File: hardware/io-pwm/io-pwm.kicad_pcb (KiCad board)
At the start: 2 copper layers, 60 x 60 mm, 30 parts, among them J1 IO EXTENSION, J2 PWM_OUT, J5 12V_A, J6 12V_B, U1 LM317T, U2 74LS164, U3 TLC7226A, U4 LM339, U5 LM555

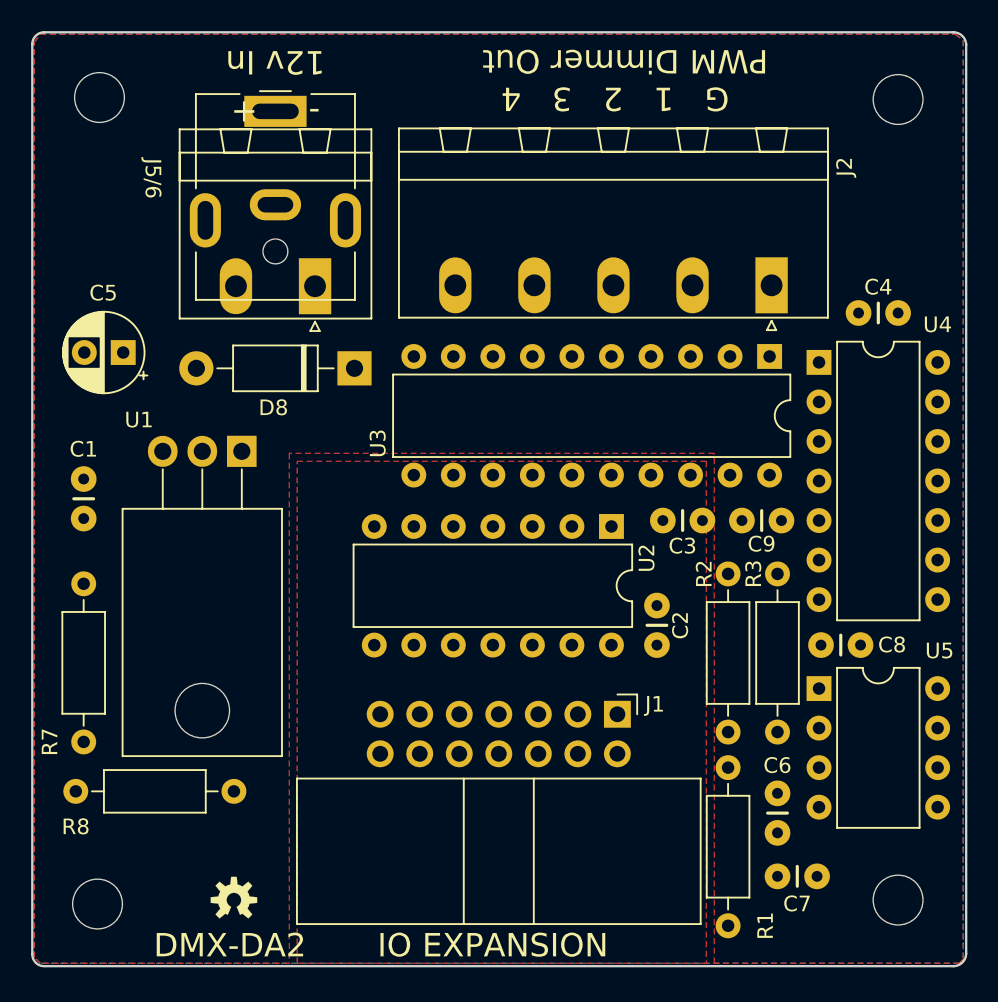
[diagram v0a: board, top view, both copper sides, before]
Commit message: Prototype version of DMX, Analog, and PWM IO Modules and both TX and RX IO interfaces.
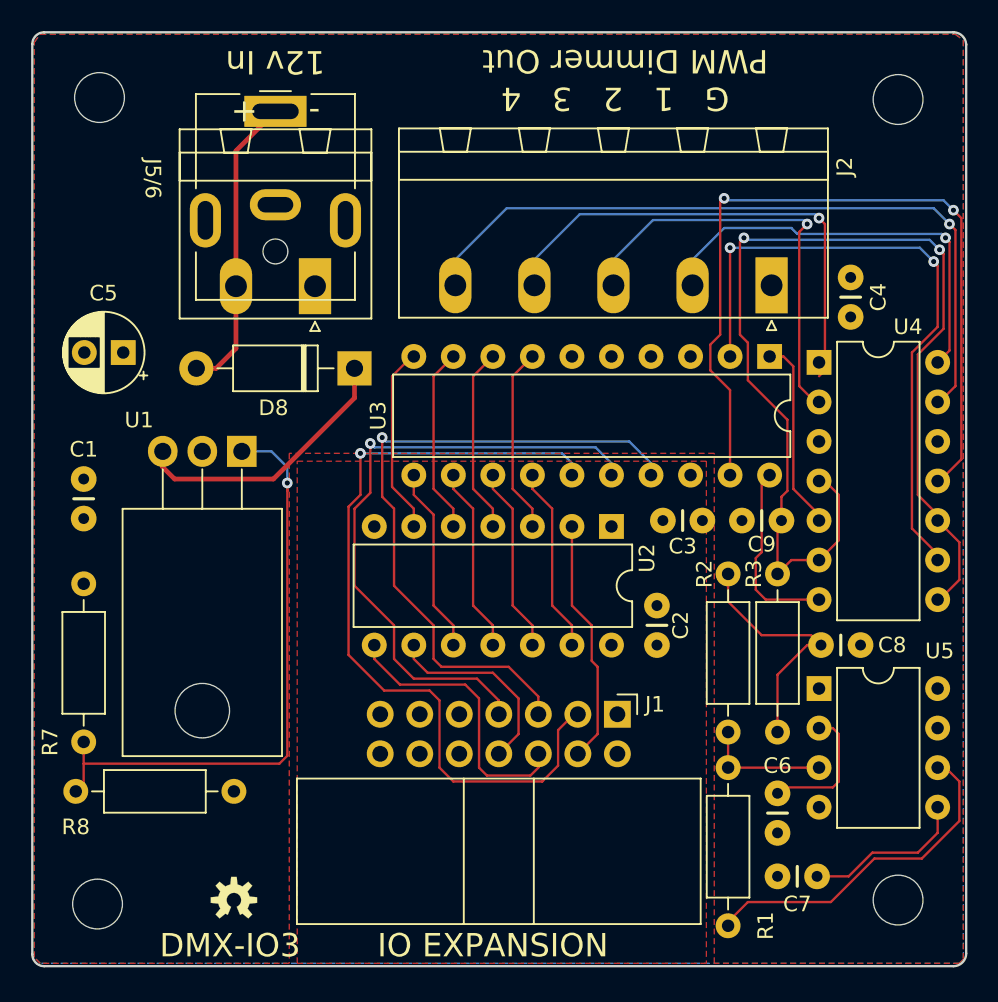
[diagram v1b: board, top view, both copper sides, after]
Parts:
- moved C4 2.05 mm to (167.0, 77.6), turned to 90 degrees
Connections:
- net Net-(J1-Pad4) renamed /SR-OUT
- net Net-(J1-Pad6) renamed /SR-CLK
- net Net-(J1-Pad8) renamed /~SR_CLR
- U2 pad 10: Net-(U2-Pad10) -> /D3
- U2 pad 11: Net-(U2-Pad11) -> /D2
- U2 pad 12: Net-(U2-Pad12) -> /D1
- U2 pad 13: Net-(U2-Pad13) -> /D0
- U2 pad 3: Net-(U2-Pad3) -> /D7
- U2 pad 4: Net-(U2-Pad4) -> /D6
- U2 pad 5: Net-(U2-Pad5) -> /D5
- U2 pad 6: Net-(U2-Pad6) -> /D4
- U3 pad 10: Net-(U2-Pad10) -> /D4
- U3 pad 11: Net-(U2-Pad6) -> /D3
- U3 pad 12: Net-(U2-Pad5) -> /D2
- U3 pad 13: Net-(U2-Pad4) -> /D1
- U3 pad 14: Net-(U2-Pad3) -> /D0
- U3 pad 7: Net-(U2-Pad13) -> /D7
- U3 pad 8: Net-(U2-Pad12) -> /D6
- U3 pad 9: Net-(U2-Pad11) -> /D5
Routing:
- net Net-(C9-Pad1): track 0.00 -> 70.7 mm, vias 0 -> 2
- net /AO3: track 0.00 -> 52.0 mm, vias 0 -> 2
- net /~WR: track 0.00 -> 51.8 mm, vias 0 -> 1
- net Net-(J2-Pad5): track 0.00 -> 47.3 mm, vias 0 -> 1
- net /A0: track 0.00 -> 43.2 mm, vias 0 -> 1
- net /AO0: track 0.00 -> 41.8 mm, vias 0 -> 2
- net /A1: track 0.00 -> 40.8 mm, vias 0 -> 1
- net Net-(R7-Pad1): track 0.00 -> 38.7 mm, vias 0 -> 1
- net Net-(J2-Pad4): track 0.00 -> 31.7 mm, vias 0 -> 1
- net Net-(J2-Pad3): track 0.00 -> 27.6 mm, vias 0 -> 1
- net Net-(J2-Pad2): track 0.00 -> 27.4 mm, vias 0 -> 1
- net Net-(R1-Pad1): track 0.00 -> 22.1 mm
- net Net-(D8-Pad2): track 0.00 -> 20.2 mm
- net /SR-CLK: track 0.00 -> 18.2 mm
- net Net-(D8-Pad1): track 0.00 -> 17.7 mm
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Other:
- net class Power added: clearance 0.1524, trace_width 0.3048, via_dia 1.27, via_drill 0.635
- board text added: "DMX-IO3"
- board text added: "DMX-IO3, Rev 1.1 Crazy Giraffe Software"
- board text removed: "DMX-DA2"
- board text removed: "DMX-DA2, Rev 1.1 Crazy Giraffe Software"
